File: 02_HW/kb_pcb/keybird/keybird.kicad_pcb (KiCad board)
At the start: 2 copper layers, 145.4 x 141.3 mm, 73 parts, among them J1 Adafruit_Feather_16_pin, J2 Adafruit_feather_12_pin, J4 FTDI UART, SW1 SW_Push, SW10 SW_Push, SW11 SW_Push, SW12 SW_Push, SW13 SW_Push, SW14 SW_Push, SW15 SW_Push, SW16 SW_Push, SW17 SW_Push, SW18 SW_Push, SW19 SW_Push, SW2 SW_Push, SW20 SW_Push, SW21 SW_Push, SW22 SW_Push, SW23 SW_Push, SW24 SW_Push, SW25 SW_Push, SW26 SW_Push, SW27 SW_Push, SW28 SW_Push, SW29 SW_Push, SW3 SW_Push, SW30 SW_Push, SW4 SW_Push, SW5 Power enable, SW6 SW_Push, SW7 SW_Push, SW8 SW_Push, SW9 SW_Push

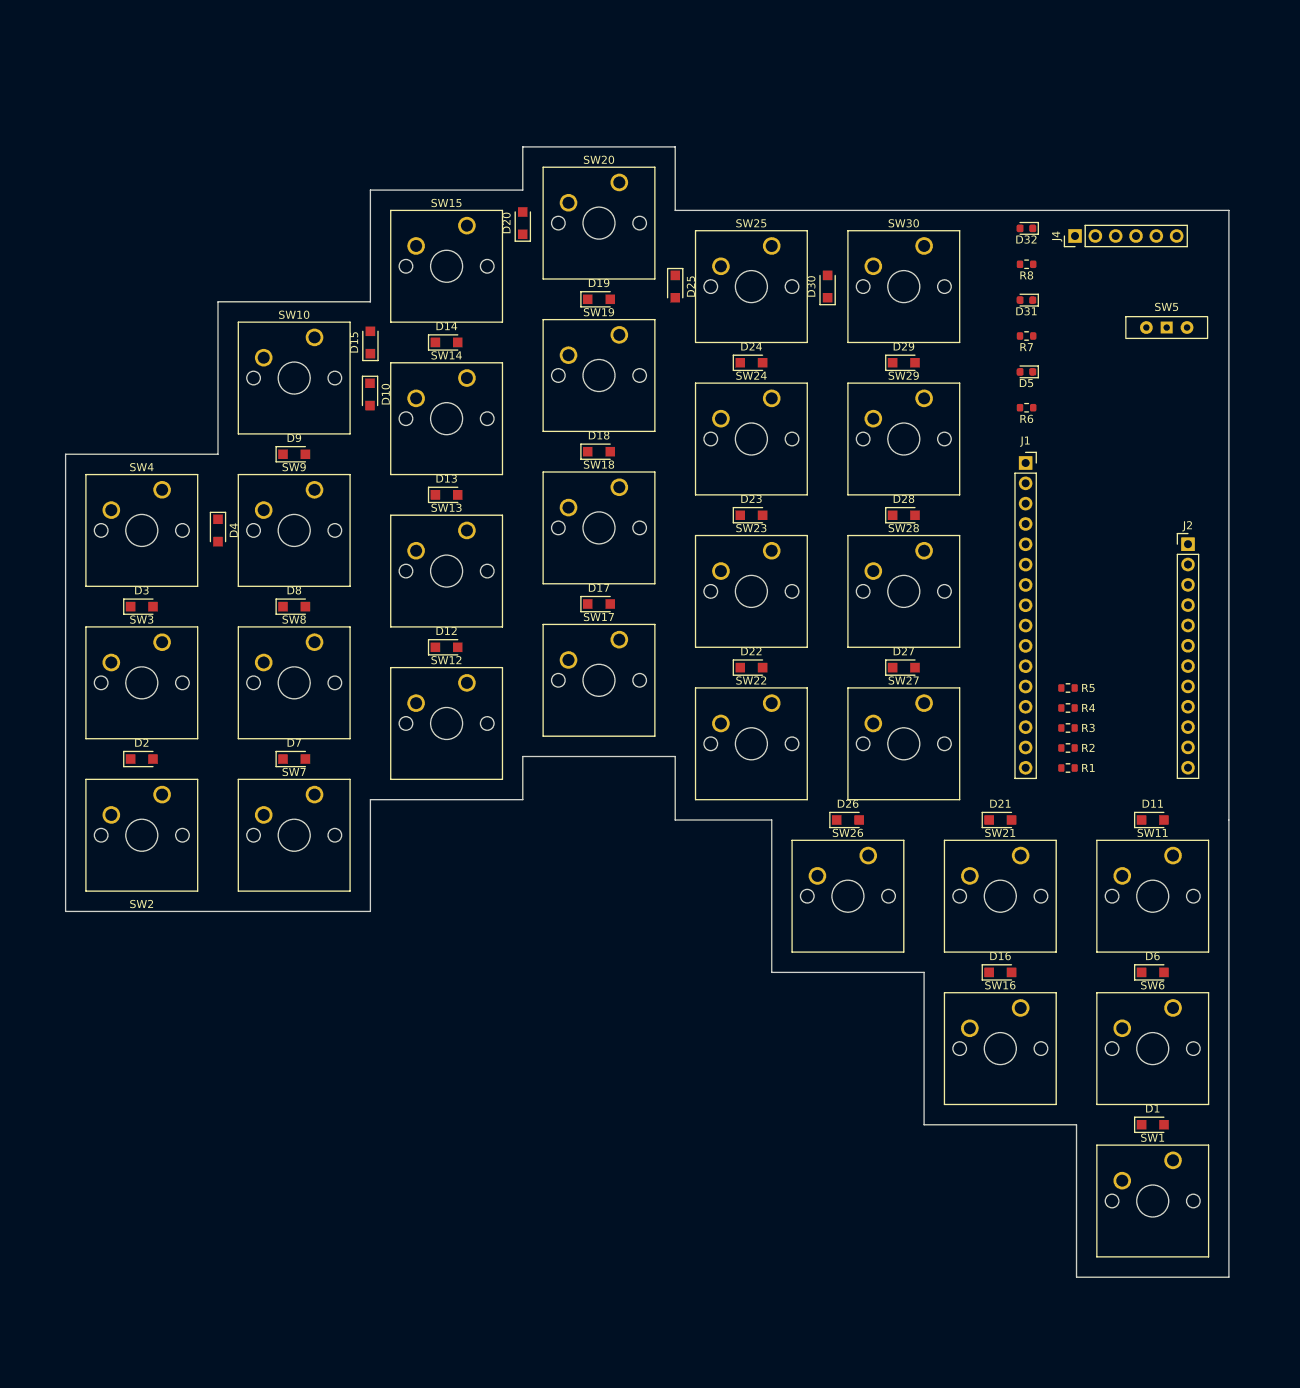
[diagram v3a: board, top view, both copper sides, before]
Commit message: Trimmed down board shape, completed tracing, adding ground pours and via stitching
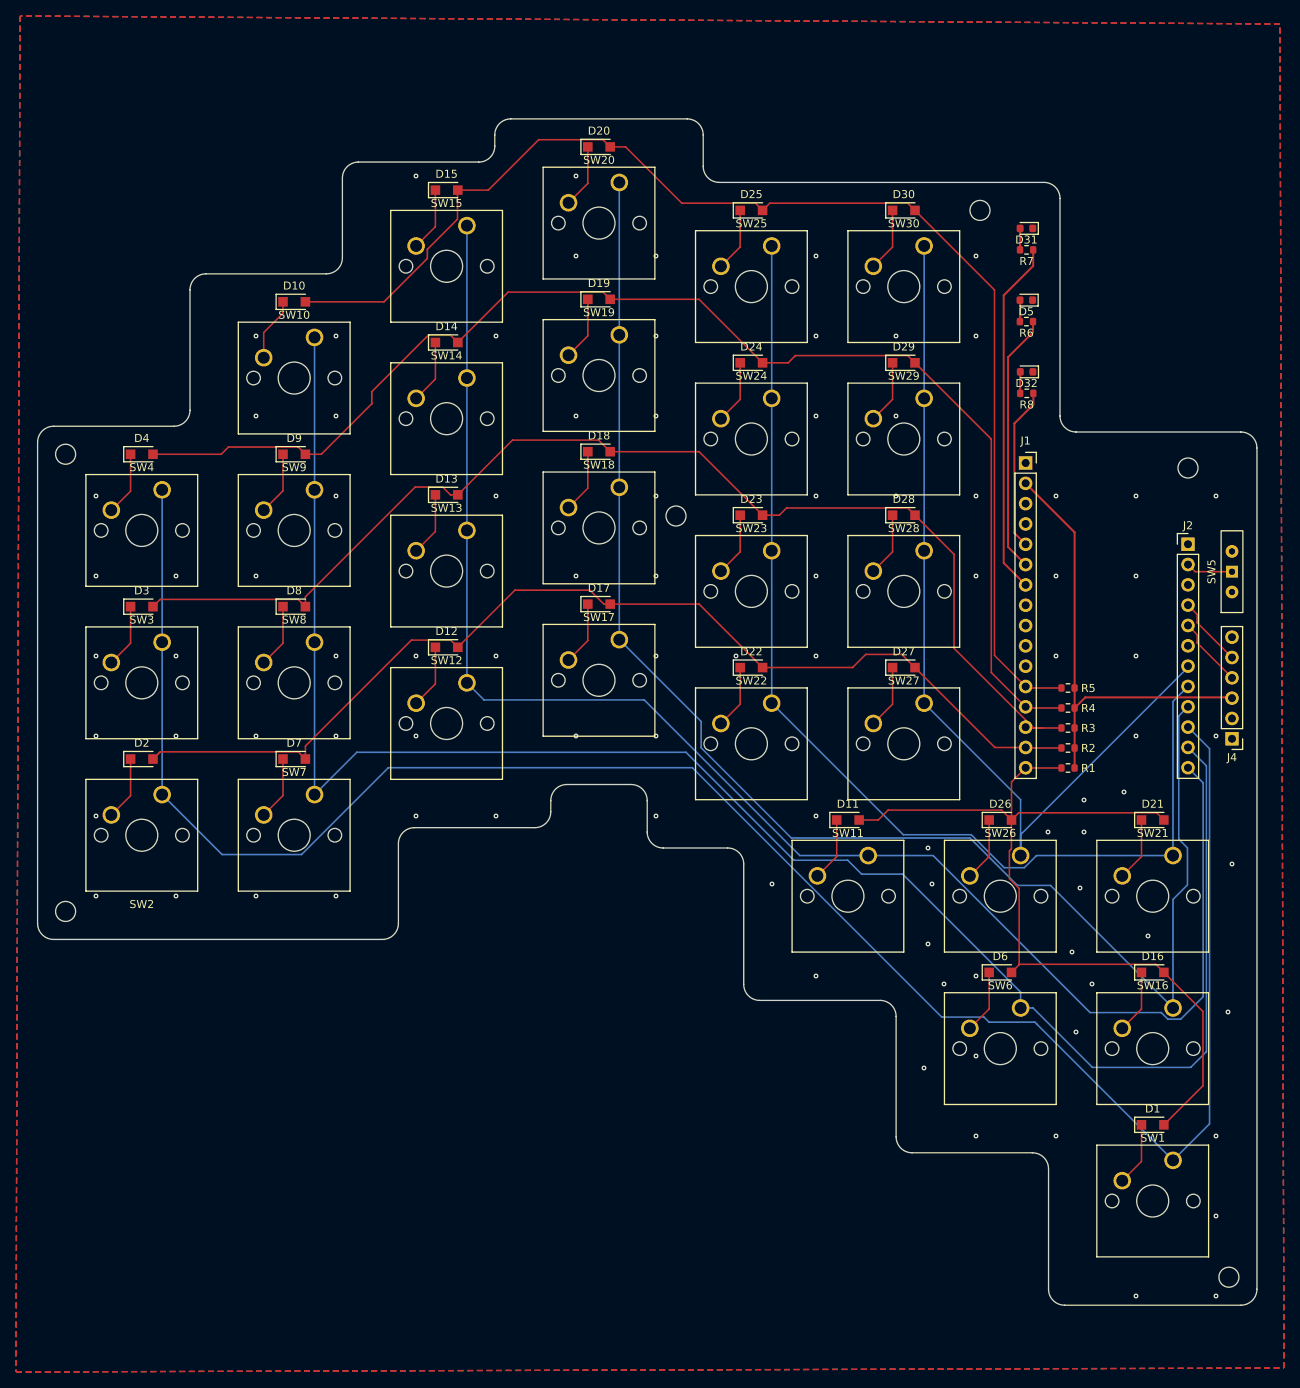
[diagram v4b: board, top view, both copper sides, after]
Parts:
- added H1: MountingHole, MountingHole:MountingHole_2.5mm, F.Cu at (20.7, 131.4)
- added H2: MountingHole, MountingHole:MountingHole_2.5mm, F.Cu at (166.1, 177.2)
- added H3: MountingHole, MountingHole:MountingHole_2.5mm, F.Cu at (20.7, 74.3)
- added H4: MountingHole, MountingHole:MountingHole_2.5mm, F.Cu at (97.0, 82.0)
- added H5: MountingHole, MountingHole:MountingHole_2.5mm, F.Cu at (135.0, 43.8)
- added H6: MountingHole, MountingHole:MountingHole_2.5mm, F.Cu at (161.0, 76.0)
- moved J4 65.8 mm to (166.5, 109.8), turned to 180 degrees
- moved D11 38.1 mm to (118.5, 120.0)
- moved SW11 38.1 mm to (121.0, 124.4)
- moved SW5 31.6 mm to (166.5, 89.0), turned to 90 degrees
- moved D15 21.3 mm to (68.3, 41.3), turned to 0 degrees
- moved D16 19.1 mm to (156.6, 139.1)
- moved D21 19.1 mm to (156.6, 120.0)
- moved D6 19.1 mm to (137.5, 139.1)
- moved SW26 19.1 mm to (140.1, 124.4)
- moved D26 19.0 mm to (137.5, 120.0)
- moved SW16 19.0 mm to (159.1, 143.5)
- moved SW21 19.0 mm to (159.1, 124.4)
- moved SW6 19.0 mm to (140.1, 143.5)
- moved D32 17.9 mm to (140.8, 64.0)
- moved R8 16.1 mm to (140.8, 66.7)
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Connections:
- J1 pad 6: /BLUE_LED -> /GREEN_LED
- J1 pad 7: /GREEN_LED -> /BLUE_LED
- J2 pad 10: /Col_2 -> /Col_0
- J2 pad 12: /Col_0 -> /Col_2
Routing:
- net /Col_0: track 0.00 -> 249.6 mm
- net /Col_1: track 0.00 -> 228.1 mm
- net /Col_2: track 0.00 -> 197.2 mm
- net /Col_3: track 0.00 -> 187.0 mm
- net /Row_3: track 0.00 -> 163.8 mm
- net /Row_4: track 0.00 -> 161.6 mm
- net /Row_2: track 0.00 -> 149.3 mm
- net /Col_4: track 0.00 -> 138.6 mm
- net /Row_1: track 0.00 -> 134.3 mm
- net /Col_5: track 0.00 -> 113.5 mm
- net /Row_0: track 0.00 -> 113.3 mm
- net +3.3V: track 0.00 -> 58.4 mm
- net /BLUE_LED: track 0.00 -> 44.5 mm
- net /GREEN_LED: track 0.00 -> 32.6 mm
- net /RED_LED: track 0.00 -> 20.4 mm
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- added copper zone on B.Cu, net GNDREF
- added copper zone on F.Cu, net GNDREF
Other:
- board size 145.4 x 141.3 mm -> 152.4 x 148.3 mm

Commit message: Resolved design rule conflicts
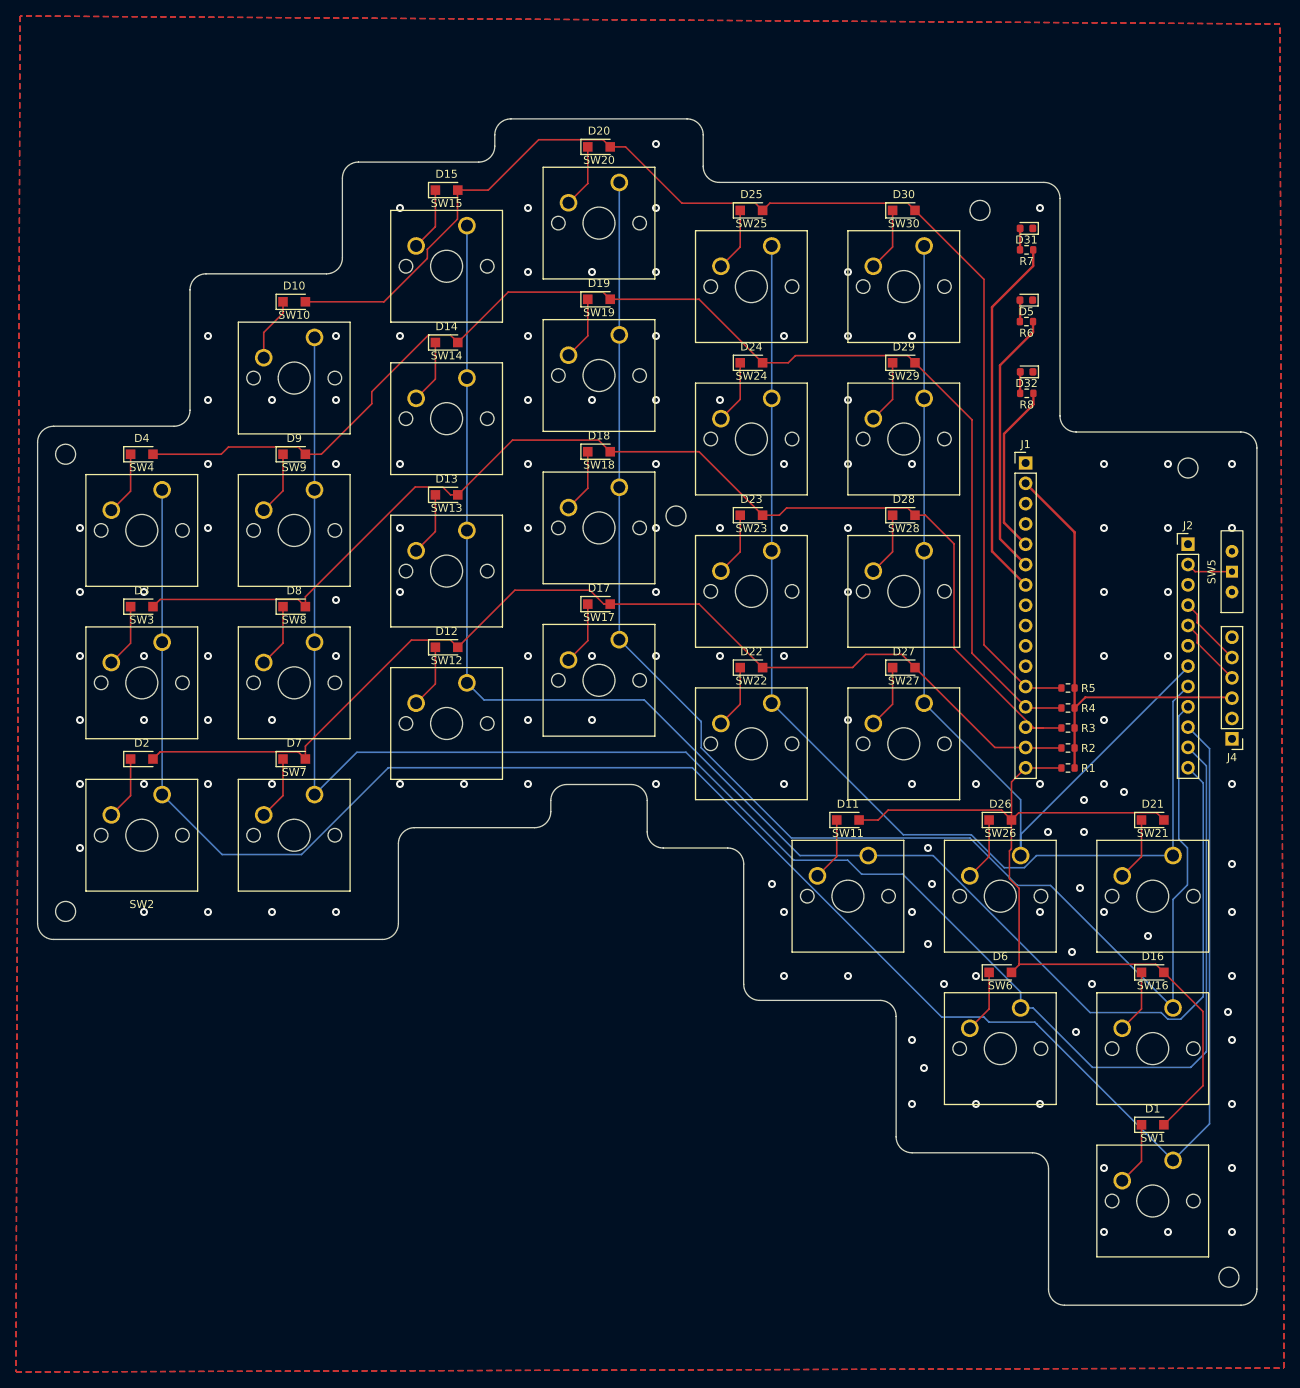
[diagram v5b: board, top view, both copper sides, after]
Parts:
- J1: footprint Connector_PinSocket_2.54mm:PinSocket_1x16_P2.54mm_Vertical -> Connector_PinHeader_2.54mm:PinHeader_1x16_P2.54mm_Vertical
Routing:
- net /BLUE_LED: track 44.5 -> 45.8 mm
- net /RED_LED: track 20.4 -> 21.5 mm
- net /GREEN_LED: track 32.6 -> 33.4 mm
- net /Row_2: track 149.3 -> 149.9 mm
- net GNDREF: vias 92 -> 130
